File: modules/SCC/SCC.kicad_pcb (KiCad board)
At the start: 2 copper layers, 160 x 100 mm, 19 parts, among them J1 CardConnector, J2 CPU GRANT CONFIGURATION, U1 74AHCT541, U2 74AHCT541, U3 74AHCT245, U4 74AHCT541, U5 74AHCT541, U6 74HCT10, U7 W65C02, Y1 1Mhz

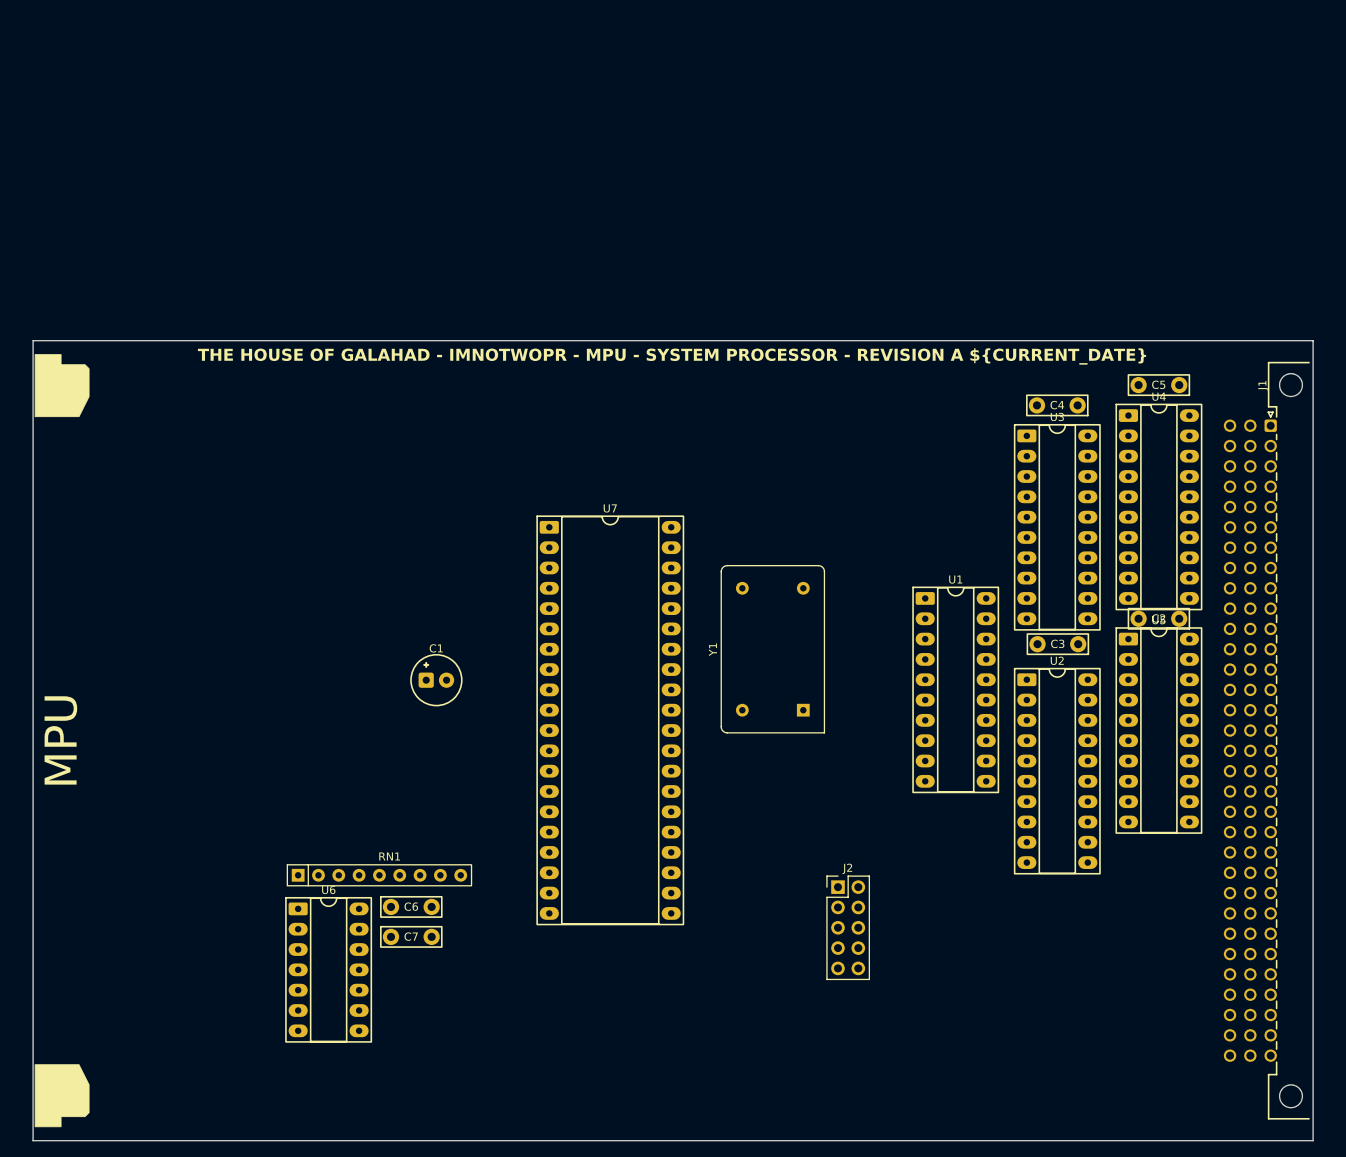
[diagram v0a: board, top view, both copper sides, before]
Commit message: migrated PWR to SCC; updates to MPU, more work pending
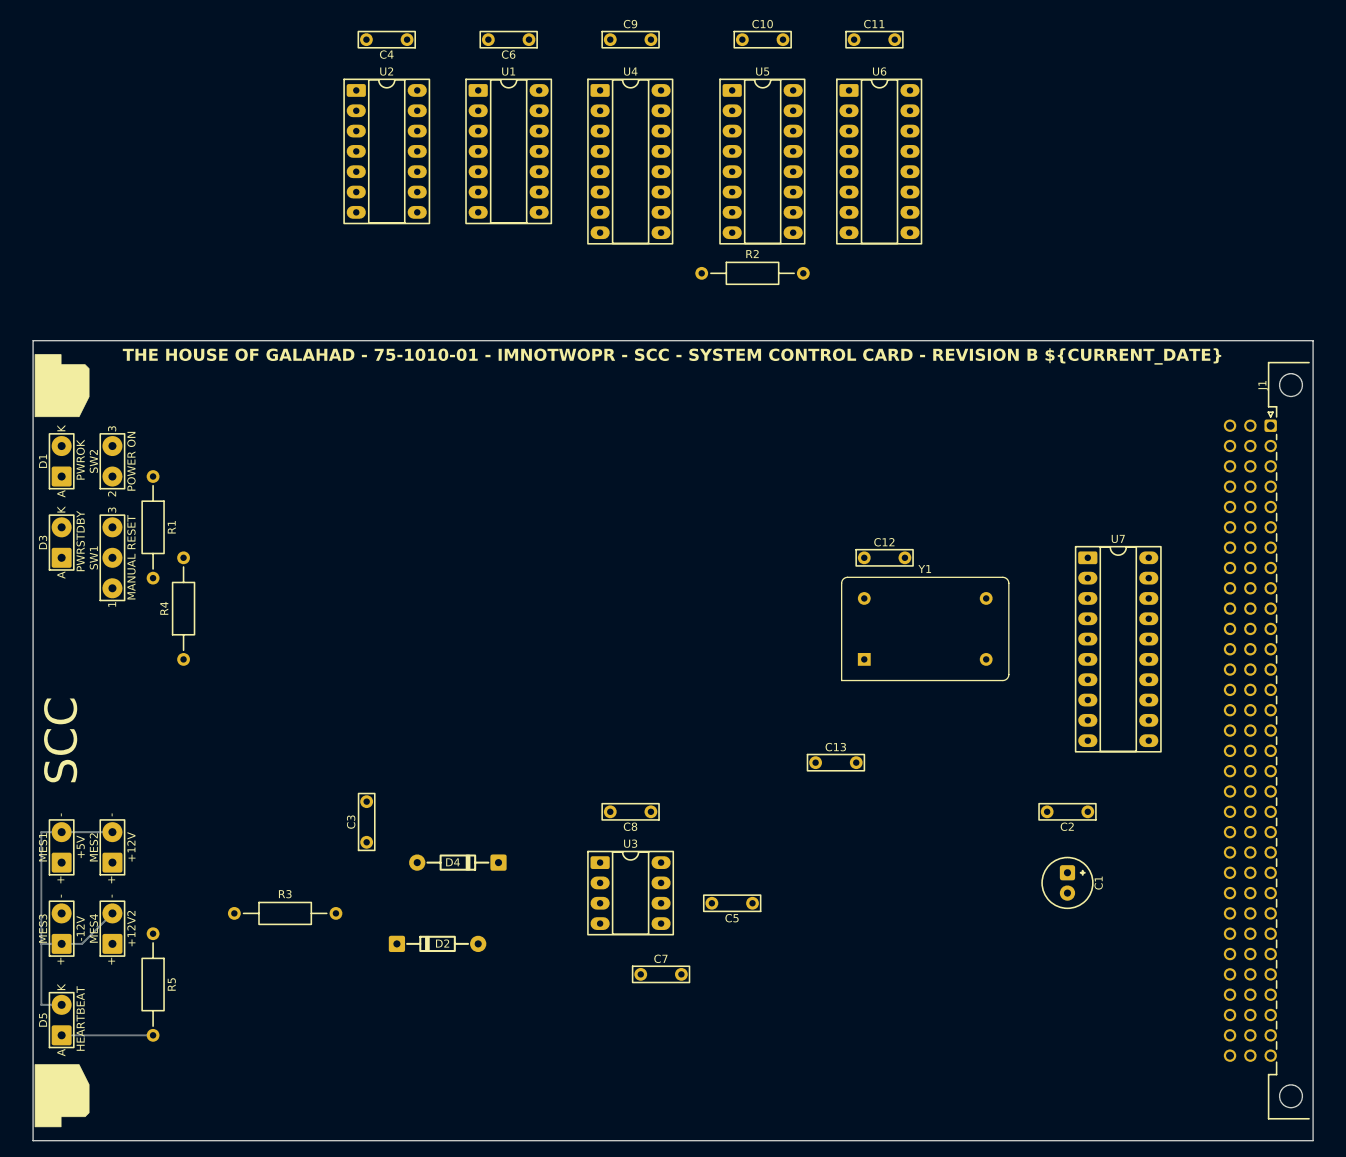
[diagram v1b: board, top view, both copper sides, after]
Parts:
- removed J2: CPU GRANT CONFIGURATION, Connector_PinHeader_2.54mm:PinHeader_2x05_P2.54mm_Vertical
- removed RN1: 10k, Resistor_THT:R_Array_SIP9
- added C10: 100n, IMNOTWOPR:C_Rect_P200mil, F.Cu at (146.2, 7.37)
- added C11: 100n, IMNOTWOPR:C_Rect_P200mil, F.Cu at (160.2, 7.37)
- added C12: 100n, IMNOTWOPR:C_Rect_P200mil, F.Cu at (161.4, 72.1)
- added C13: 100n, IMNOTWOPR:C_Rect_P200mil, F.Cu at (155.4, 97.7)
- added C8: 100n, IMNOTWOPR:C_Rect_P200mil, F.Cu at (129.7, 103.9)
- added C9: 100n, IMNOTWOPR:C_Rect_P200mil, F.Cu at (129.7, 7.37)
- added D1: LED_G, IMNOTWOPR:Wire_LED, F.Cu at (58.6, 60.1)
- added D2: 1N4148, FormantKO:DO-35_P400mil, F.Cu at (105.6, 120.4)
- added D3: LED_R, IMNOTWOPR:Wire_LED, F.Cu at (58.6, 70.2)
- added D4: 1N4148, FormantKO:DO-35_P400mil, F.Cu at (108.1, 110.2)
- added D5: LED, IMNOTWOPR:Wire_LED, F.Cu at (58.6, 129.9)
- added MES1: Voltmeter_DC, IMNOTWOPR:Wire_Meter, F.Cu at (58.6, 108.3)
- added MES2: Voltmeter_DC, IMNOTWOPR:Wire_Meter, F.Cu at (64.9, 108.3)
- added MES3: Voltmeter_DC, IMNOTWOPR:Wire_Meter, F.Cu at (58.6, 118.5)
- added MES4: Voltmeter_DC, IMNOTWOPR:Wire_Meter, F.Cu at (64.9, 118.5)
- added R1: 430R, IMNOTWOPR:R_Axial_DIN0207_P400mil, F.Cu at (70.0, 68.3)
- added R2: 10k, IMNOTWOPR:R_Axial_DIN0207_P400mil, F.Cu at (144.9, 36.6)
- added R3: 91k, IMNOTWOPR:R_Axial_DIN0207_P400mil, F.Cu at (86.5, 116.6)
- added R4: 430R, IMNOTWOPR:R_Axial_DIN0207_P400mil, F.Cu at (73.8, 78.5)
- added R5: 430R, IMNOTWOPR:R_Axial_DIN0207_P400mil, F.Cu at (70.0, 125.5)
- added SW1: 1MS2T1B1M1QES, IMNOTWOPR:Wire_SW_SPDT, F.Cu at (64.9, 72.1)
- added SW2: 1MS1T1B1M1QES, IMNOTWOPR:Wire_SW_SPST_23, F.Cu at (64.9, 60.1)
- C1: value 47u -> 47µF
- C2, C4, C6: footprint FormantKO:C_Rect_P200mil -> IMNOTWOPR:C_Rect_P200mil
- C3, C7: value 100n -> 10n; footprint FormantKO:C_Rect_P200mil -> IMNOTWOPR:C_Rect_P200mil
- C5: value 100n -> 1u; footprint FormantKO:C_Rect_P200mil -> IMNOTWOPR:C_Rect_P200mil
- U1: value 74AHCT541 -> 74HCT14; footprint IMNOTWOPR:DIP-20N -> IMNOTWOPR:DIP-14N
- U2: value 74AHCT541 -> 74HCT00; footprint IMNOTWOPR:DIP-20N -> IMNOTWOPR:DIP-14N
- U3: value 74AHCT245 -> 555; footprint IMNOTWOPR:DIP-20N -> IMNOTWOPR:DIP-8N
- U4, U5: value 74AHCT541 -> 74HCT390; footprint IMNOTWOPR:DIP-20N -> IMNOTWOPR:DIP-16N
- U6: value 74HCT10 -> 74HCT390; footprint IMNOTWOPR:DIP-14N -> IMNOTWOPR:DIP-16N
- U7: value W65C02 -> 74AHCT541; footprint IMNOTWOPR:DIP-40W -> IMNOTWOPR:DIP-20N
- moved U6 122.3 mm to (160.8, 22.6)
- moved U2 114.1 mm to (99.2, 21.3)
- moved C6 109.1 mm to (114.5, 7.37), turned to 180 degrees
- moved C4 95.5 mm to (99.2, 7.37)
- moved C3 89.2 mm to (96.7, 105.2), turned to 90 degrees
- moved U1 87.5 mm to (114.5, 21.3)
- moved U5 86.7 mm to (146.2, 22.6)
- moved C5 83.9 mm to (142.4, 115.3)
- moved C1 82.9 mm to (184.3, 112.8), turned to -90 degrees
- moved U4 78.9 mm to (129.7, 22.6)
- moved U3 70.3 mm to (129.7, 114.0)
- moved U7 64.1 mm to (190.7, 83.6)
- moved C7 31.6 mm to (133.5, 124.2)
- moved C2 26.7 mm to (184.3, 103.9)
- moved Y1 9.92 mm to (158.9, 84.8), turned to 0 degrees
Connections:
- C1 pad 1: +5V -> +5VSB
- C2 pad 1: +5V -> +5VSB
- C3 pad 1: +5V -> Net-(C3-Pad1)
- C3 pad 2: GND -> Net-(D2-A)
- C4 pad 1: +5V -> +5VSB
- C5 pad 1: +5V -> Net-(U3-DISCH)
- C6 pad 1: +5V -> +5VSB
- C7 pad 1: +5V -> Net-(U3-CONT)
- J1 pad a10: /SA6 -> unconnected-(J1A-A_{6}-Pada10)
- J1 pad a11: /SA7 -> unconnected-(J1A-A_{7}-Pada11)
- J1 pad a12: /SA8 -> unconnected-(J1A-A_{8}-Pada12)
- J1 pad a13: /SA9 -> unconnected-(J1A-A_{9}-Pada13)
- J1 pad a14: /SA10 -> unconnected-(J1A-A_{10}-Pada14)
- J1 pad a15: /SA11 -> unconnected-(J1A-A_{11}-Pada15)
- J1 pad a16: /SA12 -> unconnected-(J1A-A_{12}-Pada16)
- J1 pad a17: /SA13 -> unconnected-(J1A-A_{13}-Pada17)
- J1 pad a18: /SA14 -> unconnected-(J1A-A_{14}-Pada18)
- J1 pad a19: /SA15 -> unconnected-(J1A-A_{15}-Pada19)
- J1 pad a3: unconnected-(J1A-+12V-Pada3) -> +12V
- J1 pad a30: unconnected-(J1A-+12V-Pada30) -> +12V
- J1 pad a4: /SA0 -> unconnected-(J1A-A_{0}-Pada4)
- J1 pad a5: /SA1 -> unconnected-(J1A-A_{1}-Pada5)
- J1 pad a6: /SA2 -> unconnected-(J1A-A_{2}-Pada6)
- J1 pad a7: /SA3 -> unconnected-(J1A-A_{3}-Pada7)
- J1 pad a8: /SA4 -> unconnected-(J1A-A_{4}-Pada8)
- J1 pad a9: /SA5 -> unconnected-(J1A-A_{5}-Pada9)
- J1 pad b10: Net-(J1B-READY) -> unconnected-(J1B-READY-Padb10)
- J1 pad b11: Net-(J1B-BE) -> unconnected-(J1B-BE-Padb11)
- J1 pad b12: Net-(J1B-SYNC) -> unconnected-(J1B-SYNC-Padb12)
- J1 pad b13: Net-(J1B-VPB) -> unconnected-(J1B-VPB-Padb13)
- J1 pad b14: Net-(J1B-MLB) -> unconnected-(J1B-MLB-Padb14)
- J1 pad b15: unconnected-(J1B-VDA-Padb15) -> /RESET
- J1 pad b22: /SD0 -> unconnected-(J1B-D_{0}-Padb22)
- J1 pad b23: /SD1 -> unconnected-(J1B-D_{1}-Padb23)
- J1 pad b24: /SD2 -> unconnected-(J1B-D_{2}-Padb24)
- J1 pad b25: /SD3 -> unconnected-(J1B-D_{3}-Padb25)
- J1 pad b26: /SD4 -> unconnected-(J1B-D_{4}-Padb26)
- J1 pad b27: /SD5 -> unconnected-(J1B-D_{5}-Padb27)
- J1 pad b28: /SD6 -> unconnected-(J1B-D_{6}-Padb28)
- J1 pad b29: /SD7 -> unconnected-(J1B-D_{7}-Padb29)
- J1 pad b3: unconnected-(J1B--12V-Padb3) -> -12V
- J1 pad b30: unconnected-(J1B--12V-Padb30) -> -12V
- J1 pad b4: Net-(J1B-/VALID) -> PHI2_B0
- J1 pad b5: Net-(J1B-PHI2) -> unconnected-(J1B-PHI2-Padb5)
- J1 pad b6: Net-(J1B-R/W) -> unconnected-(J1B-R~{W}-Padb6)
- J1 pad b7: Net-(J1B-/RESET) -> unconnected-(J1B-~{RESET}-Padb7)
- J1 pad b8: Net-(J1B-/IRQ) -> unconnected-(J1B-~{IRQ}-Padb8)
- J1 pad b9: Net-(J1B-/NMI) -> unconnected-(J1B-~{NMI}-Padb9)
- J1 pad c1: unconnected-(J1C-+5VSB-Padc1) -> +5VSB
- J1 pad c21: Net-(J1C-/BUSGNT0) -> unconnected-(J1C-~{BUSGNT0}-Padc21)
- J1 pad c23: Net-(J1C-/BUSGNT1) -> unconnected-(J1C-~{BUSGNT1}-Padc23)
- J1 pad c26: Net-(J1C-/BUSGNT2) -> unconnected-(J1C-~{BUSGNT2}-Padc26)
- J1 pad c28: Net-(J1C-/BUSGNT3) -> unconnected-(J1C-~{BUSGNT3}-Padc28)
- J1 pad c3: unconnected-(J1C-+12V2-Padc3) -> +12V2
- J1 pad c30: unconnected-(J1C-+12V2-Padc30) -> +12V2
- J1 pad c4: unconnected-(J1C-/PSON-Padc4) -> /PSON
- J1 pad c5: unconnected-(J1C-PWROK-Padc5) -> PWROK
- U1 pad 1: //CPU_GRANT -> PWROK
- U1 pad 10: GND -> unconnected-(U1-Pad10)
- U1 pad 11: unconnected-(U1A-Y7-Pad11) -> GND
- U1 pad 13: Net-(J1B-MLB) -> GND
- U1 pad 14: Net-(J1B-VPB) -> +5VSB
- U1 pad 2: //VALID -> Net-(C3-Pad1)
- U1 pad 3: /PHI2 -> Net-(U3-OUT)
- U1 pad 4: /R/W -> Net-(D4-A)
- U1 pad 5: /SYNC -> GND
- U1 pad 6: /VPB -> unconnected-(U1-Pad6)
- U1 pad 7: /MLB -> GND
- U1 pad 8: GND -> unconnected-(U1-Pad8)
- U2 pad 1: //VALID -> PWROK
- U2 pad 10: GND -> +5VSB
- U2 pad 12: unconnected-(U2A-Y6-Pad12) -> GND
- U2 pad 13: unconnected-(U2A-Y5-Pad13) -> GND
- U2 pad 14: /BE -> +5VSB
- U2 pad 2: Net-(J1B-/RESET) -> PWROK
- U2 pad 3: Net-(J1B-/IRQ) -> Net-(U2-Pad3)
- U2 pad 4: Net-(J1B-/NMI) -> Net-(U2-Pad4)
- U2 pad 5: Net-(J1B-READY) -> Net-(U2-Pad4)
- U2 pad 6: Net-(J1B-BE) -> Net-(R4-Pad1)
- U2 pad 8: GND -> Net-(U2-Pad4)
- U2 pad 9: GND -> Net-(U2-Pad3)
- U3 pad 1: /R/W -> GND
- U3 pad 2: /SD0 -> Net-(D2-A)
- U3 pad 3: /SD1 -> Net-(U3-OUT)
- U3 pad 4: /SD2 -> +5VSB
- U3 pad 5: /SD3 -> Net-(U3-CONT)
- U3 pad 6: /SD4 -> Net-(U3-DISCH)
- U3 pad 7: /SD5 -> Net-(U3-DISCH)
- U3 pad 8: /SD6 -> +5VSB
- U4 pad 1: //CPU_GRANT -> Net-(U4A-Q3)
- U4 pad 10: GND -> unconnected-(U4B-Q2-Pad10)
- U4 pad 11: /SA7 -> unconnected-(U4B-Q1-Pad11)
- U4 pad 12: /SA6 -> Net-(U4A-Q0)
- U4 pad 13: /SA5 -> Net-(U4B-Q0)
- U4 pad 14: /SA4 -> GND
- U4 pad 15: /SA3 -> Net-(U4B-Q3)
- U4 pad 16: /SA2 -> +5VSB
- U4 pad 2: /A0 -> GND
- U4 pad 3: /A1 -> Net-(U4A-Q0)
- U4 pad 4: /A2 -> PHI2_B1
- U4 pad 5: /A3 -> unconnected-(U4A-Q1-Pad5)
- U4 pad 6: /A4 -> unconnected-(U4A-Q2-Pad6)
- U4 pad 7: /A5 -> Net-(U4A-Q3)
- U4 pad 8: /A6 -> GND
- U4 pad 9: /A7 -> Net-(U4B-Q3)
- U5 pad 1: //CPU_GRANT -> Net-(U5A-Q3)
- U5 pad 10: GND -> unconnected-(U5B-Q2-Pad10)
- U5 pad 11: /SA15 -> unconnected-(U5B-Q1-Pad11)
- U5 pad 12: /SA14 -> Net-(U5A-Q0)
- U5 pad 13: /SA13 -> Net-(U5B-Q0)
- U5 pad 14: /SA12 -> GND
- U5 pad 15: /SA11 -> Net-(U5B-Q3)
- U5 pad 16: /SA10 -> +5VSB
- U5 pad 2: /A8 -> GND
- U5 pad 3: /A9 -> Net-(U5A-Q0)
- U5 pad 4: /A10 -> Net-(U4B-Q0)
- U5 pad 5: /A11 -> unconnected-(U5A-Q1-Pad5)
- U5 pad 6: /A12 -> unconnected-(U5A-Q2-Pad6)
- U5 pad 7: /A13 -> Net-(U5A-Q3)
- U5 pad 8: /A14 -> GND
- U5 pad 9: /A15 -> Net-(U5B-Q3)
- U6 pad 1: Net-(U6-Pad1) -> Net-(U6A-Q3)
- U6 pad 10: GND -> unconnected-(U6B-Q2-Pad10)
- U6 pad 11: GND -> unconnected-(U6B-Q1-Pad11)
- U6 pad 12: //VALID -> Net-(U6A-Q0)
- U6 pad 13: /PHI2 -> Net-(U6B-Q0)
- U6 pad 14: +5V -> GND
- U6 pad 2: //RESET -> GND
- U6 pad 3: //CPU_GRANT -> Net-(U6A-Q0)
- U6 pad 4: //CPU_GRANT -> Net-(U5B-Q0)
- U6 pad 5: //CPU_GRANT -> unconnected-(U6A-Q1-Pad5)
- U6 pad 6: Net-(U6-Pad1) -> unconnected-(U6A-Q2-Pad6)
- U6 pad 7: GND -> Net-(U6A-Q3)
- U6 pad 8: unconnected-(U6-Pad8) -> GND
- U6 pad 9: GND -> Net-(U6B-Q3)
- U7 pad 1: /VPB -> GND
- U7 pad 10: /A1 -> GND
- U7 pad 11: /A2 -> PHI2_B7
- U7 pad 12: /A3 -> PHI2_B6
- U7 pad 13: /A4 -> PHI2_B5
- U7 pad 14: /A5 -> PHI2_B4
- U7 pad 15: /A6 -> PHI2_B3
- U7 pad 16: /A7 -> PHI2_B2
- U7 pad 17: /A8 -> PHI2_B1
- U7 pad 18: /A9 -> PHI2_B0
- U7 pad 19: /A10 -> GND
- U7 pad 2: /READY -> Net-(U7A-A0)
- U7 pad 20: /A11 -> +5VSB
- U7 pad 3: unconnected-(U7-ϕ_{1}OUT-Pad3) -> Net-(U7A-A0)
- U7 pad 4: //IRQ -> Net-(U7A-A0)
- U7 pad 5: /MLB -> Net-(U7A-A0)
- U7 pad 6: //NMI -> Net-(U7A-A0)
- U7 pad 7: /SYNC -> Net-(U7A-A0)
- U7 pad 8: +5V -> Net-(U7A-A0)
- U7 pad 9: /A0 -> Net-(U7A-A0)
- Y1 pad 8: /PHI2 -> Net-(U7A-A0)
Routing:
- net GND: track 0.00 -> 43.5 mm
- net Net-(D5-A): track 0.00 -> 11.4 mm
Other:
- board text added: "${COMPANY} - ${COMMENT4} - ${COMMENT1} - ${TITLE} - ${COMMENT2} - REVISION ${REVISION} ${CURRENT_DATE}"
- board text removed: "${COMPANY} - ${COMMENT1} - ${TITLE} - ${COMMENT2} - REVISION ${REVISION} ${CURRENT_DATE}"

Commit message: SCC module revision B
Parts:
- added C14: 47µF, IMNOTWOPR:CP_Radial_Tantal_P100mil, F.Cu at (179.2, 54.4)
- added C15: 100n, IMNOTWOPR:C_Rect_P200mil, F.Cu at (185.6, 55.6)
- added C16: 47µF, IMNOTWOPR:CP_Radial_Tantal_P100mil, F.Cu at (190.7, 112.8)
- added C17: 100n, IMNOTWOPR:C_Rect_P200mil, F.Cu at (184.3, 114.0)
- moved C9 106.6 mm to (169.1, 106.4), turned to 180 degrees
- moved U4 105.4 mm to (169.1, 120.4)
- moved C11 102.0 mm to (136.0, 106.4), turned to 180 degrees
- moved U6 100.9 mm to (136.0, 120.4)
- moved C10 99.3 mm to (152.6, 106.4), turned to 180 degrees
- moved U5 98.0 mm to (152.6, 120.4)
- moved D4 82.0 mm to (188.1, 92.5)
- moved C4 72.2 mm to (86.5, 78.5)
- moved C6 71.5 mm to (106.8, 78.5)
- moved U2 71.0 mm to (86.5, 91.2)
- moved U1 70.3 mm to (106.8, 91.2)
- moved C1 56.6 mm to (193.2, 56.9)
- moved R2 52.6 mm to (103.0, 68.3)
- moved C2 48.2 mm to (199.5, 58.2), turned to -90 degrees
- moved D2 47.1 mm to (101.8, 73.4), turned to 180 degrees
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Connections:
- C10 pad 1: +5VSB -> +5V
- C11 pad 1: +5VSB -> +5V
- C13 pad 1: +5VSB -> +5V
- C9 pad 1: +5VSB -> +5V
- U4 pad 16: +5VSB -> +5V
- U5 pad 16: +5VSB -> +5V
- U6 pad 16: +5VSB -> +5V
- U7 pad 20: +5VSB -> +5V
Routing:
- net GND: track 43.5 -> 647.6 mm
- net +5V: track 0.00 -> 346.3 mm
- net +12V: track 0.00 -> 255.9 mm
- net -12V: track 0.00 -> 227.7 mm
- net +12V2: track 0.00 -> 214.9 mm
- net +5VSB: track 0.00 -> 196.6 mm
- net PWROK: track 0.00 -> 148.0 mm
- net /PSON: track 0.00 -> 142.3 mm
- net Net-(D4-A): track 0.00 -> 80.5 mm
- net Net-(D2-A): track 0.00 -> 76.3 mm
- net Net-(U6B-Q0): track 0.00 -> 69.6 mm
- net PHI2_B1: track 0.00 -> 61.9 mm, vias 0 -> 1
- net PHI2_B0: track 0.00 -> 35.3 mm
- net Net-(U7A-A0): track 0.00 -> 34.3 mm
- net Net-(U5B-Q0): track 0.00 -> 25.2 mm
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- added copper zone on B.Cu, net +5V
- added copper zone on F.Cu, net +5VSB
- added copper zone on B.Cu, net GND
- added copper zone on F.Cu, net GND
